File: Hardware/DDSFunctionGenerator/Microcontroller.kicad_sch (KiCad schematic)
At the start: 19 parts, among them J8 Conn_01x04_Female, J9 Conn_01x04_Female, U5 STM32F030K6Tx, Y1 20MHz

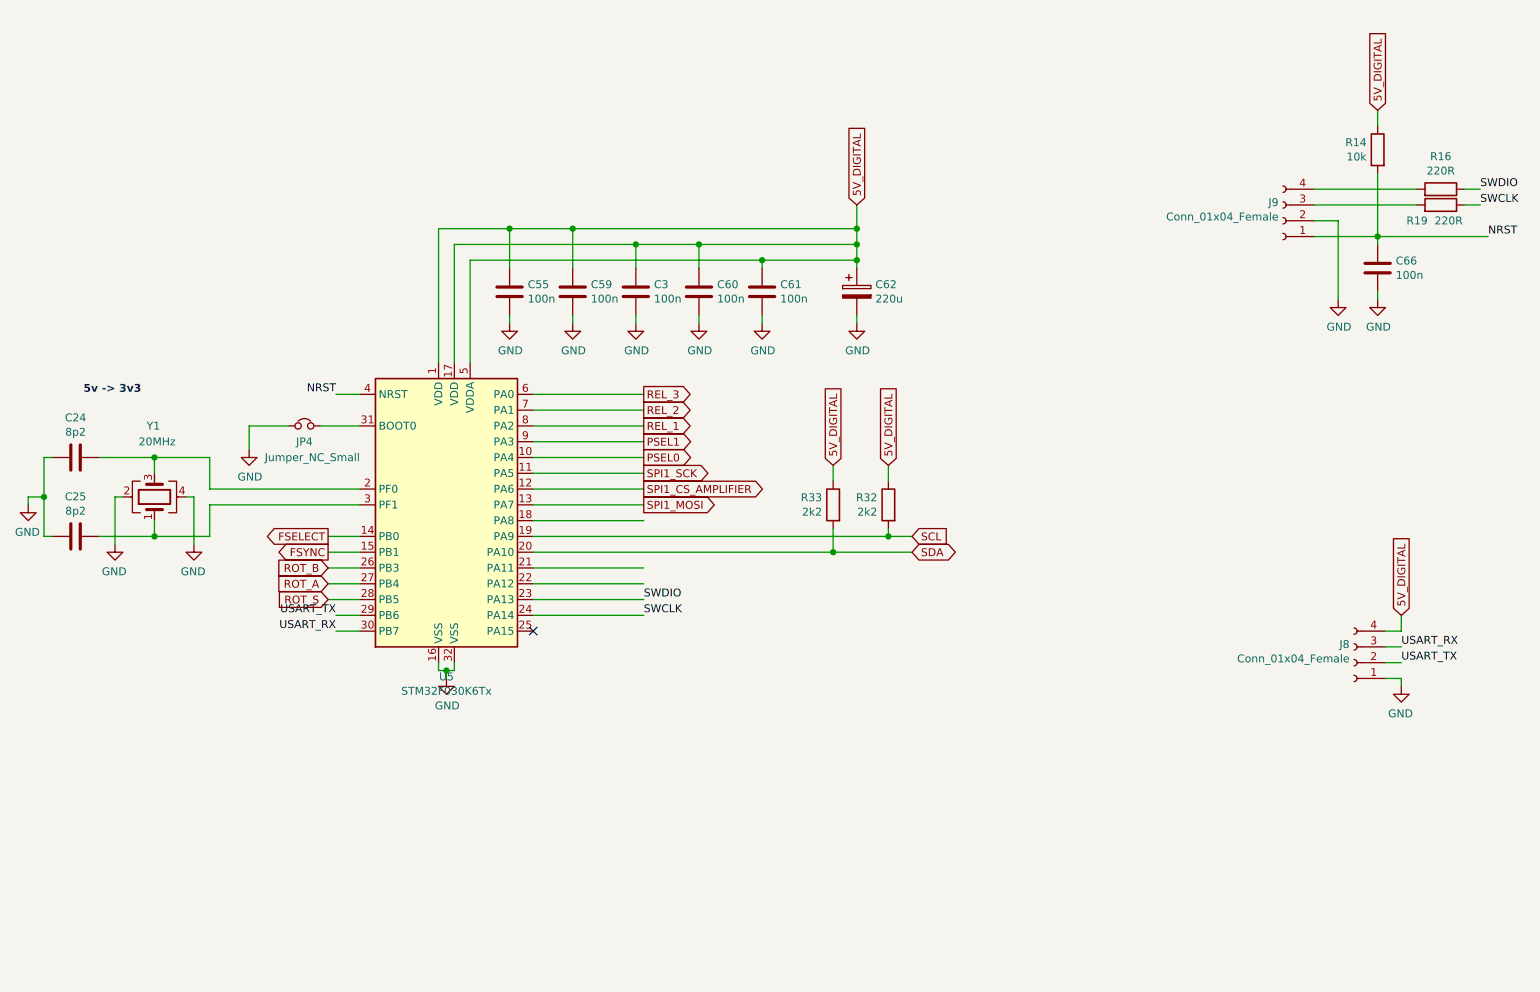
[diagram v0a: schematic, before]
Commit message: move to raspbbery pico, first draft
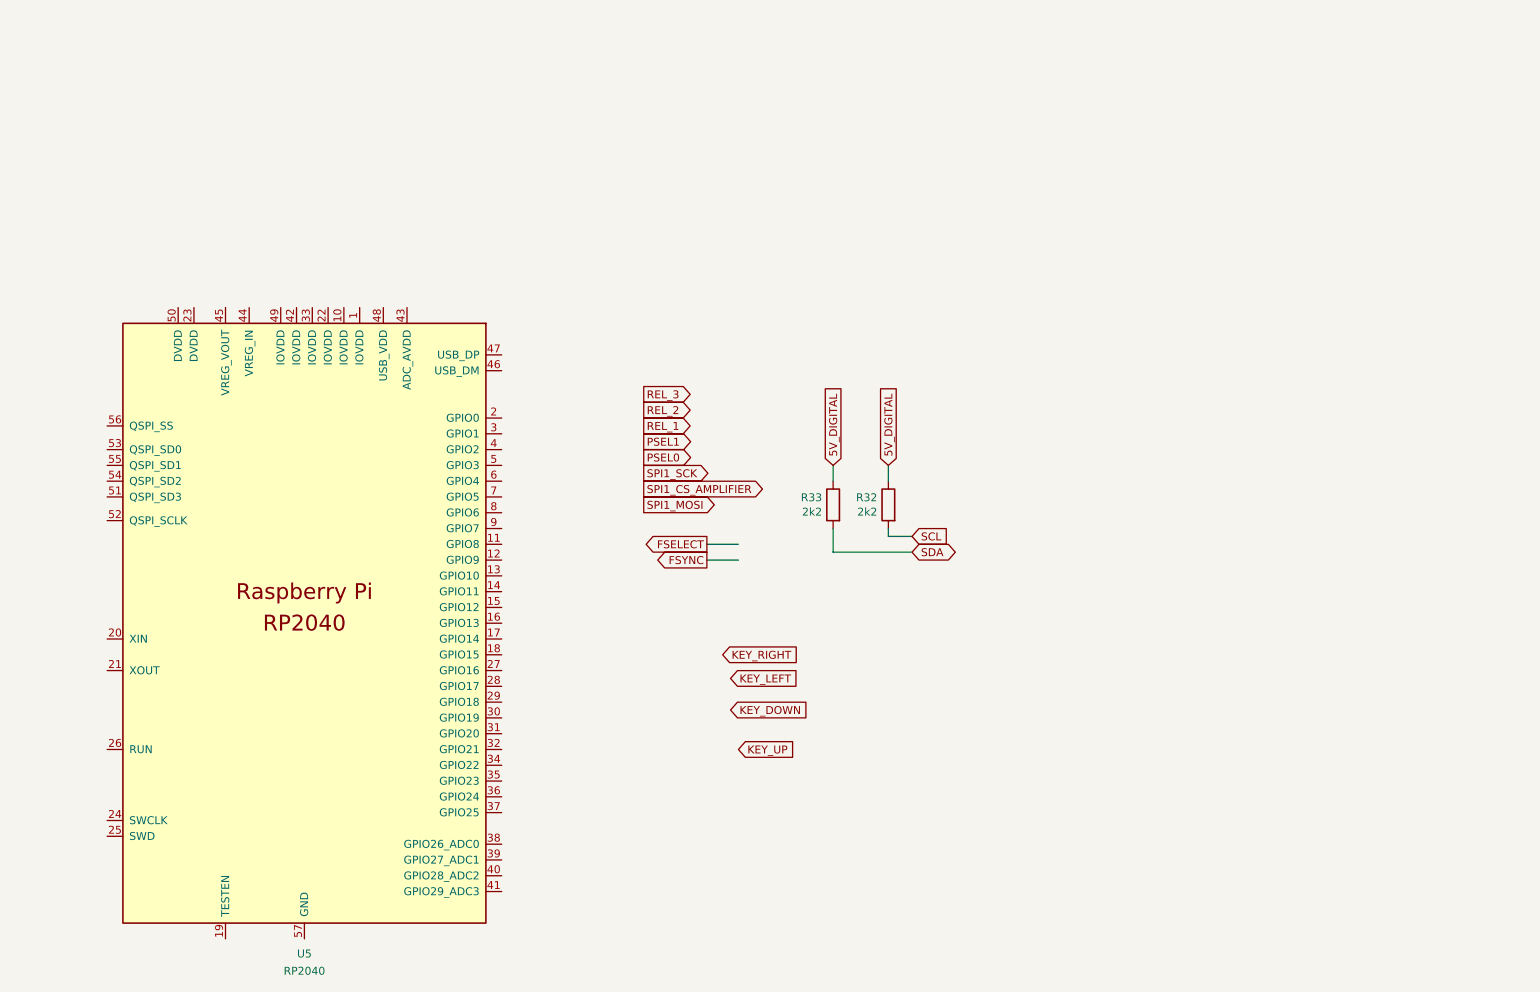
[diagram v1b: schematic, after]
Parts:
- removed C24, C25: 8p2, Capacitor_SMD:C_0402_1005Metric, symbol Device:C
- removed C3, C55, C59, C60, C61, C66: 100n, Capacitor_SMD:C_0402_1005Metric, symbol Device:C
- removed C62: 220u, Capacitor_SMD:CP_Elec_6.3x5.8, symbol Device:CP
- removed J8, J9: Conn_01x04_Female, Connector_PinHeader_2.54mm:PinHeader_1x04_P2.54mm_Vertical, symbol Connector:Conn_01x04_Female
- removed JP4: Jumper_NC_Small, Jumper:SolderJumper-2_P1.3mm_Bridged2Bar_RoundedPad1.0x1.5mm, symbol Device:Jumper_NC_Small
- removed R14: 10k, Resistor_SMD:R_0402_1005Metric, symbol Device:R
- removed R16, R19: 220R, Resistor_SMD:R_0402_1005Metric, symbol Device:R
- removed U5: STM32F030K6Tx, Package_QFP:LQFP-32_7x7mm_P0.8mm, symbol MCU_ST_STM32F0:STM32F030K6Tx
- removed Y1: 20MHz, Oscillator:Oscillator_SMD_EuroQuartz_XO53-4Pin_5.0x3.2mm, symbol Device:Crystal_GND24
- added U5: RP2040, MCU_RaspberryPi_and_Boards:RPi_Pico_SMD_TH, symbol MCU_RaspberryPi_and_Boards:RP2040
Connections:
- no-connect marks 1 -> 0
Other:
- note removed: "5v -> 3v3"
